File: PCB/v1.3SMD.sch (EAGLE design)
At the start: 34 parts, among them IC2 ATMEGA328PUA

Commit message: added resistors
added resistors to data lines for current limitation. You could also add
capacitors in order to have a low pass filter but I rely on the gat
input capacity of the ICs instead.
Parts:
- added R19, R20, R5, R6, R7, R8, R9: 82k, rcl:R-EU_R0603
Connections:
- removed net I1: SV2.3
- removed net I2: SV2.1
- removed net I3: SV2.4
- new net LE: R19.1, U$1.LE, U$2.LE
- new net LE_M: IC2.(SS)PB2, R19.2
- new net MISO: R6.1, U$2.SDO
- new net MISO_M: IC2.(MISO)PB4, R6.2, SV2.1
- new net MOSI: R7.1, U$1.SDI
- new net MOSI_M: IC2.(MOSI)PB3, R7.2, SV2.4
- new net N$10: IC2.(ADC5)PC5
- new net N$12: IC2.(ADC4)PC4
- new net N$13: IC2.(AIN1)PD7
- new net N$17: IC2.(TXD)PD1
- new net N$18: IC2.(RXD)PD0
- new net N$19: IC2.ADC6
- new net N$20: IC2.ADC7
- new net N$22: U$1.SDO, U$2.SDI
- new net PWCLK: R20.1, U$1.PWCLK, U$2.PWCLK
- new net PWCLK_M: IC2.(T1)PD5, R20.2
- new net SCK: R5.1, U$1.CLK, U$2.CLK
- new net SCK_M: IC2.(SCK)PB5, R5.2, SV2.3
- new net SCL_M: IC2.(ICP)PB0, R9.2
- new net SDA_M: IC2.(OC1)PB1, R8.2
- net RE1_1: now also IC2.(ADC0)PC0); no longer IC2.(SCK)PB5
- net RE1_2: now also IC2.(ADC1)PC1; no longer IC2.(MISO)PB4
- net RE2_1: now also IC2.(INT0)PD2; no longer IC2.(ADC1)PC1
- net RE2_2: now also IC2.(INT1)PD3; no longer IC2.(ADC0)PC0)
- net SCL: now also R9.1; no longer IC2.(ICP)PB0
- net SDA: now also R8.1; no longer IC2.(OC1)PB1
- net SEVS3_1: now also U$2.OUT9; no longer U$2.OUT0
- net SEVS3_2: now also U$2.OUT8; no longer U$2.OUT1
- net SEVS3_3: now also U$2.OUT7; no longer U$2.OUT2
- net SEVS3_4: now also U$2.OUT6; no longer U$2.OUT3
- net SEVS3_5: now also U$2.OUT11; no longer U$2.OUT4
- net SEVS3_6: now also U$2.OUT10; no longer U$2.OUT5
- net SEVS3_7: now also U$2.OUT5; no longer U$2.OUT6
- net SEVS3_8: now also U$2.OUT4; no longer U$2.OUT7
- net SEVS4_1: now also U$2.OUT13; no longer U$2.OUT8
- net SEVS4_2: now also U$2.OUT12; no longer U$2.OUT9
- net SEVS4_3: now also U$2.OUT3; no longer U$2.OUT10
- net SEVS4_4: now also U$2.OUT2; no longer U$2.OUT11
- net SEVS4_5: now also U$2.OUT15; no longer U$2.OUT12
- net SEVS4_6: now also U$2.OUT14; no longer U$2.OUT13
- net SEVS4_7: now also U$2.OUT1; no longer U$2.OUT14
- net SEVS4_8: now also U$2.OUT0; no longer U$2.OUT15
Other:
- moved on the sheet: R18

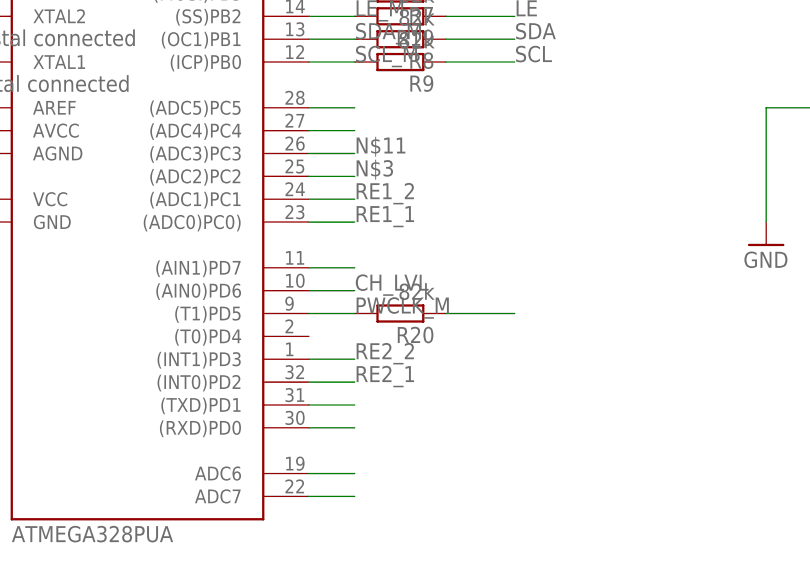
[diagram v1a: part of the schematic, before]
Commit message: Finished routing
connected all air wires and finished placing. Still need to finish up
labels and positions in silk screen
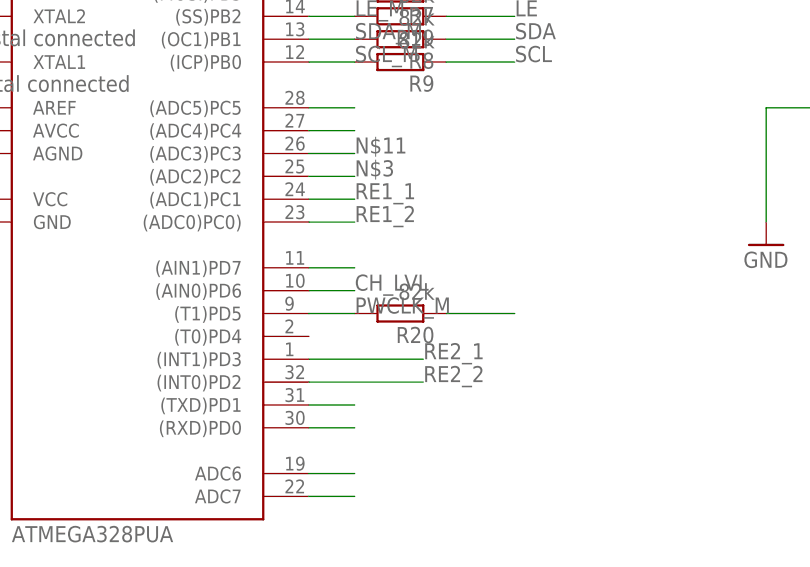
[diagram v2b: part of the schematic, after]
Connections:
- net RE1_1: now also IC2.(ADC1)PC1; no longer IC2.(ADC0)PC0)
- net RE1_2: now also IC2.(ADC0)PC0); no longer IC2.(ADC1)PC1
- net RE2_1: now also IC2.(INT1)PD3; no longer IC2.(INT0)PD2
- net RE2_2: now also IC2.(INT0)PD2; no longer IC2.(INT1)PD3
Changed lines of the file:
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@@
 <wire x1="157.48" y1="251.46" x2="157.48" y2="261.62" width="0.1524" layer="98"/>
 <wire x1="81.28" y1="335.28" x2="149.86" y2="335.28" width="0.1524" layer="98"/>
-<wire x1="149.86" y1="325.12" x2="149.86" y2="292.1" width="0.1524" layer="98"/>
-<wire x1="149.86" y1="292.1" x2="81.28" y2="292.1" width="0.1524" layer="98"/>
-<wire x1="81.28" y1="292.1" x2="81.28" y2="325.12" width="0.1524" layer="98"/>
+<wire x1="149.86" y1="325.12" x2="149.86" y2="266.7" width="0.1524" layer="98"/>
+<wire x1="149.86" y1="266.7" x2="81.28" y2="266.7" width="0.1524" layer="98"/>
+<wire x1="81.28" y1="266.7" x2="81.28" y2="325.12" width="0.1524" layer="98"/>
 <wire x1="81.28" y1="325.12" x2="81.28" y2="335.28" width="0.1524" layer="98"/>
 <wire x1="81.28" y1="325.12" x2="149.86" y2="325.12" width="0.1524" layer="98"/>
@@
 </segment>
 <segment>
-<wire x1="259.08" y1="256.54" x2="264.16" y2="256.54" width="0.1524" layer="91"/>
-<label x="264.16" y="256.54" size="1.778" layer="95"/>
-<pinref part="IC2" gate="G$1" pin="(ADC0)PC0)"/>
+<wire x1="259.08" y1="259.08" x2="264.16" y2="259.08" width="0.1524" layer="91"/>
+<label x="264.16" y="259.08" size="1.778" layer="95"/>
+<pinref part="IC2" gate="G$1" pin="(ADC1)PC1"/>
 </segment>
 </net>
@@
 </segment>
 <segment>
-<wire x1="259.08" y1="259.08" x2="264.16" y2="259.08" width="0.1524" layer="91"/>
-<label x="264.16" y="259.08" size="1.778" layer="95"/>
-<pinref part="IC2" gate="G$1" pin="(ADC1)PC1"/>
+<wire x1="259.08" y1="256.54" x2="264.16" y2="256.54" width="0.1524" layer="91"/>
+<label x="264.16" y="256.54" size="1.778" layer="95"/>
+<pinref part="IC2" gate="G$1" pin="(ADC0)PC0)"/>
 </segment>
 </net>
@@
 </segment>
 <segment>
-<pinref part="IC2" gate="G$1" pin="(INT0)PD2"/>
-<wire x1="259.08" y1="238.76" x2="264.16" y2="238.76" width="0.1524" layer="91"/>
-<label x="264.16" y="238.76" size="1.778" layer="95"/>
+<wire x1="259.08" y1="241.3" x2="271.78" y2="241.3" width="0.1524" layer="91"/>
+<label x="271.78" y="241.3" size="1.778" layer="95"/>
+<pinref part="IC2" gate="G$1" pin="(INT1)PD3"/>
 </segment>
 </net>
@@
 </segment>
 <segment>
-<pinref part="IC2" gate="G$1" pin="(INT1)PD3"/>
-<wire x1="259.08" y1="241.3" x2="264.16" y2="241.3" width="0.1524" layer="91"/>
-<label x="264.16" y="241.3" size="1.778" layer="95"/>
-</segment>
-</net>
+<wire x1="259.08" y1="238.76" x2="271.78" y2="238.76" width="0.1524" layer="91"/>
+<label x="271.78" y="238.76" size="1.778" layer="95"/>
+<pinref part="IC2" gate="G$1" pin="(INT0)PD2"/>
+</segment>
+</net>
